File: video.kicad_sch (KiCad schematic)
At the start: 1 part, among them J4 Conn_01x40_MountingPin

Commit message: save state
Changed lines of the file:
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@@
 	(bus
 		(pts
-			(xy 76.2 139.7) (xy 96.52 139.7)
+			(xy 88.9 139.7) (xy 96.52 139.7)
 		)
 		(stroke
@@
 			)
 			(justify right bottom)
-		)
-	)
-	(global_label "LCD{R[2..7] G[1..7] B[2..7] CLK DE VSYNC HSYNC PWM}"
-		(shape input)
-		(at 76.2 139.7 180)
-		(fields_autoplaced yes)
-		(effects
-			(font
-				(size 1.27 1.27)
-			)
-			(justify right)
-		)
-		(property "Intersheetrefs" "${INTERSHEET_REFS}"
-			(at 19.0279 139.7 0)
-			(hide yes)
-			(show_name no)
-			(do_not_autoplace no)
-			(effects
-				(font
-					(size 1.27 1.27)
-				)
-				(justify right)
-			)
 		)
 	)
@@
 		)
 	)
+	(hierarchical_label "LCD{R[2..7] G[1..7] B[2..7] CLK DE VSYNC HSYNC PWM}"
+		(shape bidirectional)
+		(at 88.9 139.7 180)
+		(effects
+			(font
+				(size 1.27 1.27)
+			)
+			(justify right)
+		)
+	)

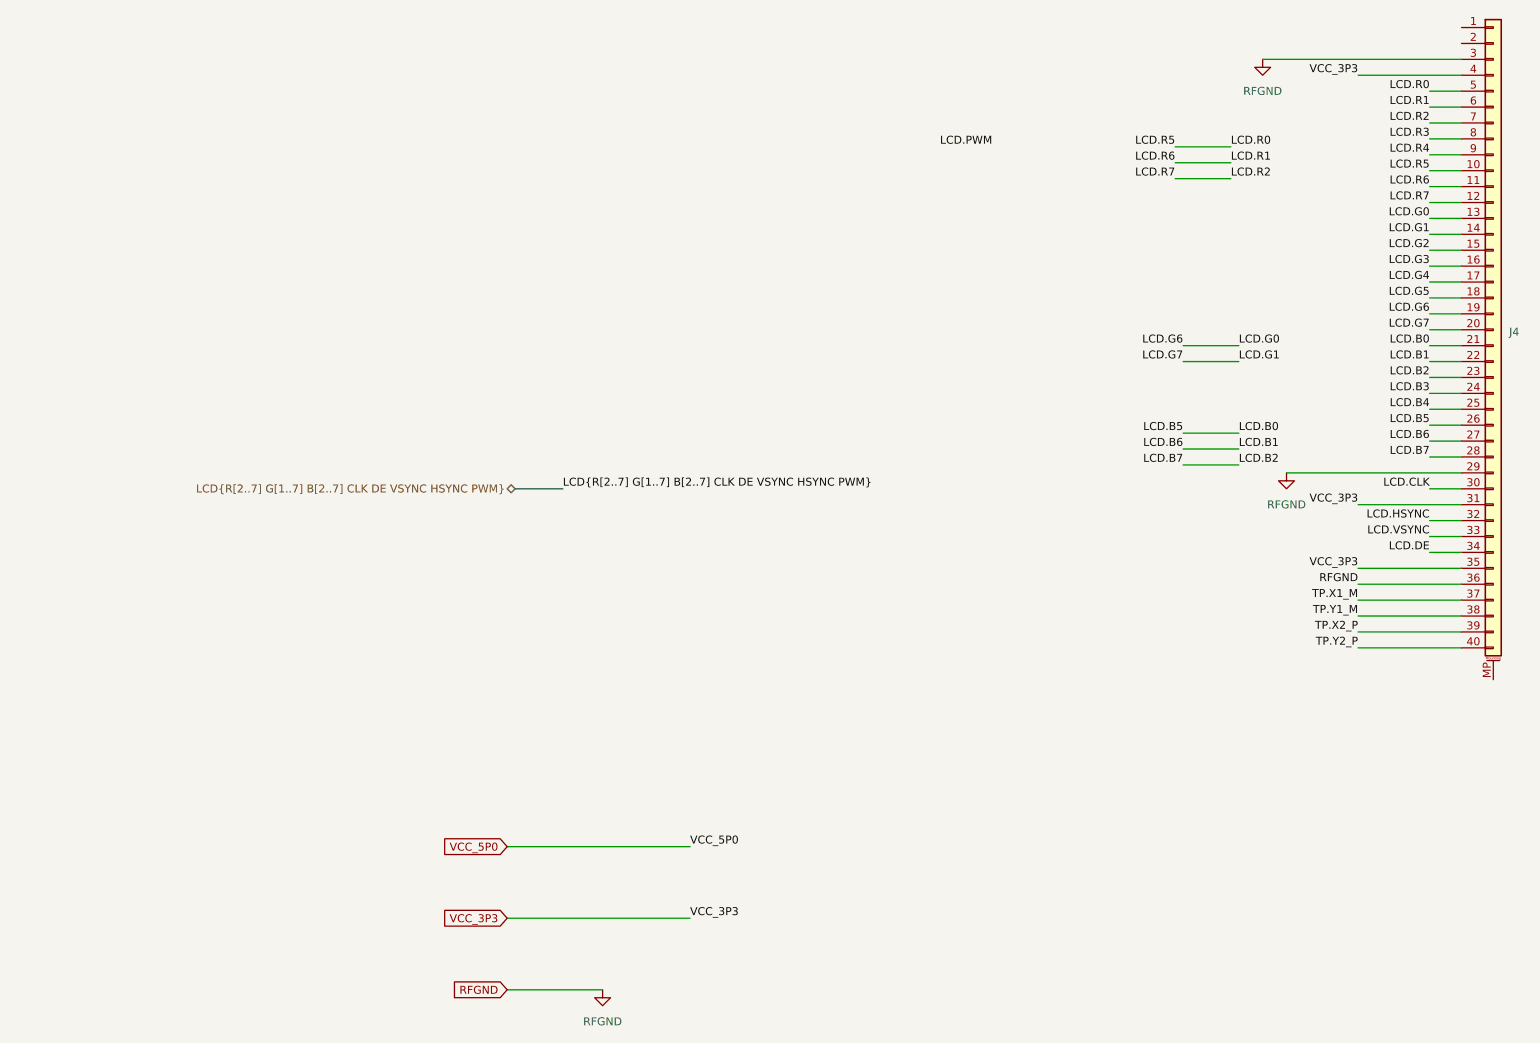
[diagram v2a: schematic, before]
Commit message: add lcd backlight chip
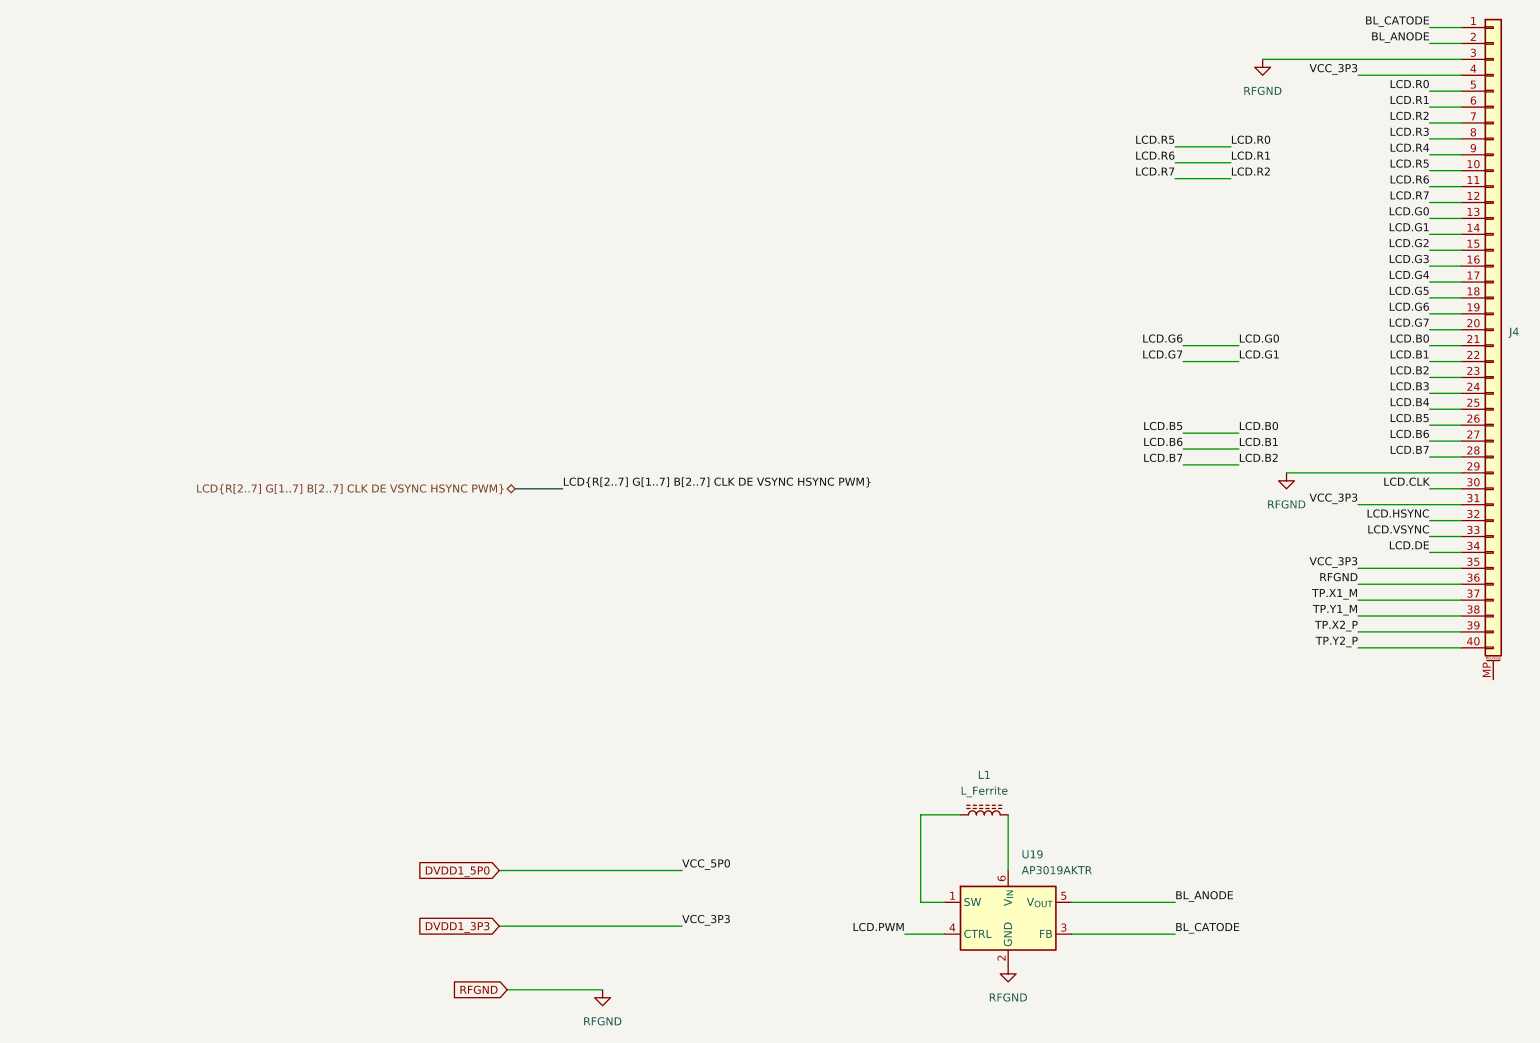
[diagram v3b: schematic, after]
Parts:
- added L1: L_Ferrite, Inductor_SMD:L_7.3x7.3_H4.5, symbol Device:L_Ferrite
- added U19: AP3019AKTR, Package_TO_SOT_SMD:SOT-23-6, symbol Driver_LED:AP3019AKTR
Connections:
- net LCD.PWM: now also U19.4 (CTRL)
- net RFGND: now also U19.2 (GND)
- net BL_CATODE: now reaches J4.1 (Pin_1)
- net BL_CATODE: now also U19.3 (FB)
- net BL_ANODE: now reaches J4.2 (Pin_2)
- net BL_ANODE: now also U19.5 (V_{OUT})
- net VCC_3P3 renamed DVDD1_3P3
- new net: L1.1, U19.1 (SW)
- new net: L1.2, U19.6 (V_{IN})
